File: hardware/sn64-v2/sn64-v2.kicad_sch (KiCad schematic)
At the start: 0 parts

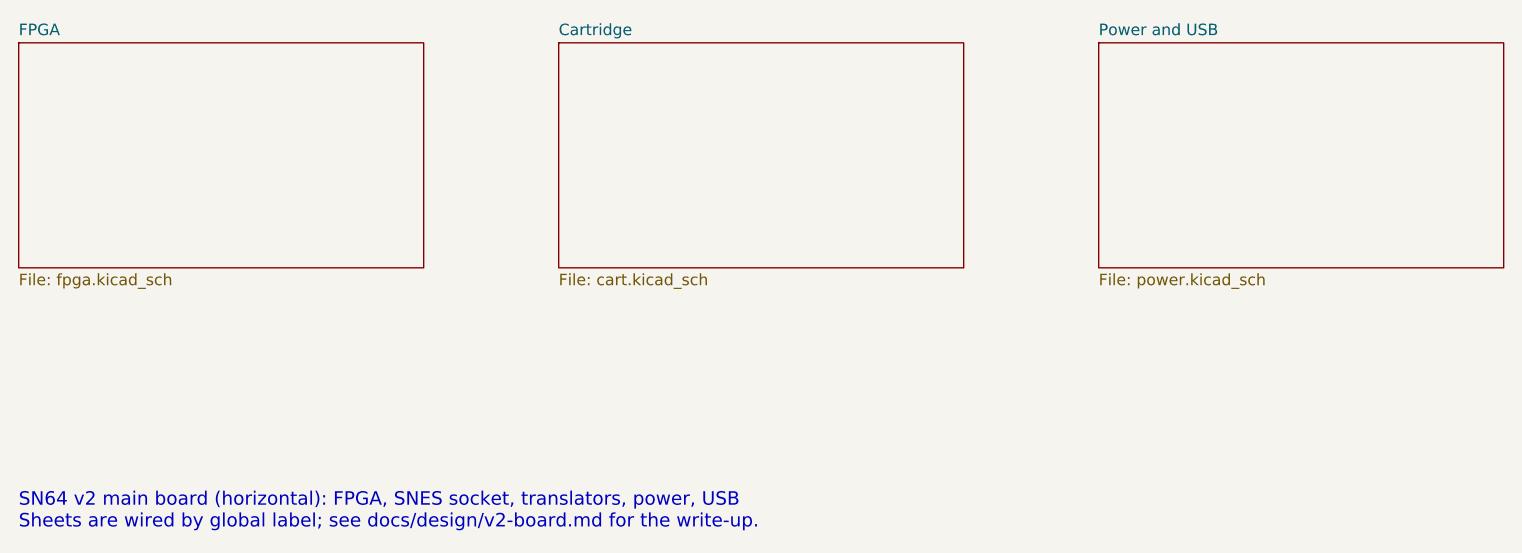
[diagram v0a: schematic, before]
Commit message: v2 single board: routed board, schematic with the N64 edge, validation reports, renders and notes
Co-Authored-By: Claude Fable 5.1 <noreply@anthropic.com>
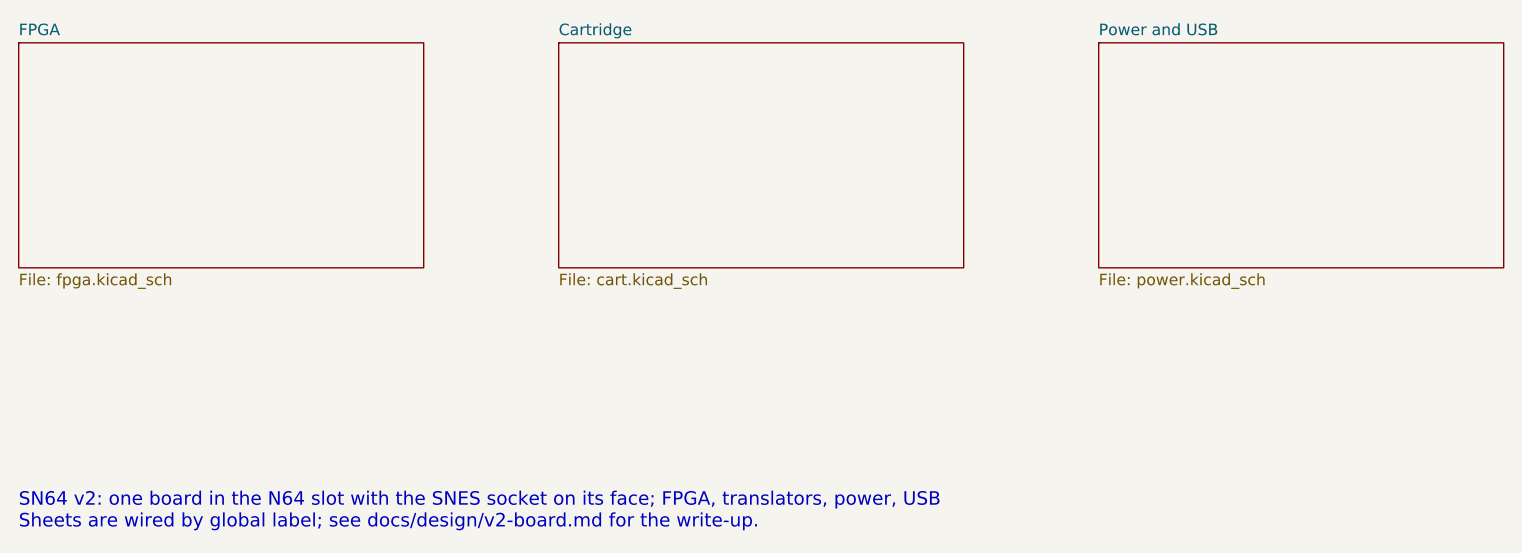
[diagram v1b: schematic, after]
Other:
- note added: "SN64 v2: one board in the N64 slot with the SNES socket on its face; FPGA, translators, power, USB Sheets are wired by global label; see docs/design/v2-board.md for the write-up."
- note removed: "SN64 v2 main board (horizontal): FPGA, SNES socket, translators, power, USB Sheets are wired by global label; see docs/design/v2-board.md for the write-up."
- title: SN64 v2 main board (horizontal): FPGA, SNES socket, translators, power, USB -> SN64 v2: one board in the N64 slot with the SNES socket on its face; FPGA, translators, power, USB
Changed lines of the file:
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@@
-(kicad_sch (version 20250114) (generator "sn64_v2_authoring") (generator_version "10.0") (paper "A4") (title_block (title "SN64 v2 main board (horizontal): FPGA, SNES socket, translators, power, USB") (date "2026-09-30") (rev "v2 draft 0.1") (comment 1 "DESIGN DRAFT - NOT FOR MANUFACTURE"))
+(kicad_sch (version 20250114) (generator "sn64_v2_authoring") (generator_version "10.0") (paper "A4") (title_block (title "SN64 v2: one board in the N64 slot with the SNES socket on its face; FPGA, translators, power, USB") (date "2026-09-30") (rev "v2 draft 0.1") (comment 1 "DESIGN DRAFT - NOT FOR MANUFACTURE"))
 (sheet (at 30 40) (size 45 25) (exclude_from_sim no) (in_bom yes) (on_board yes) (dnp no) (fields_autoplaced yes) (stroke (width 0.1524) (type solid)) (fill (color 0 0 0 0.0000)) (property "Sheetname" "FPGA" (at 30 39.3 0) (effects (font (size 1.27 1.27)) (justify left bottom))) (property "Sheetfile" "fpga.kicad_sch" (at 30 65.6 0) (effects (font (size 1.27 1.27)) (justify left top))) (instances (project "sn64-v2" (path "/d28f46aa-91c7-5060-a563-bf74d208e51e" (page "2")))))
 (sheet (at 90 40) (size 45 25) (exclude_from_sim no) (in_bom yes) (on_board yes) (dnp no) (fields_autoplaced yes) (stroke (width 0.1524) (type solid)) (fill (color 0 0 0 0.0000)) (property "Sheetname" "Cartridge" (at 90 39.3 0) (effects (font (size 1.27 1.27)) (justify left bottom))) (property "Sheetfile" "cart.kicad_sch" (at 90 65.6 0) (effects (font (size 1.27 1.27)) (justify left top))) (instances (project "sn64-v2" (path "/d28f46aa-91c7-5060-a563-bf74d208e51e" (page "3")))))
 (sheet (at 150 40) (size 45 25) (exclude_from_sim no) (in_bom yes) (on_board yes) (dnp no) (fields_autoplaced yes) (stroke (width 0.1524) (type solid)) (fill (color 0 0 0 0.0000)) (property "Sheetname" "Power and USB" (at 150 39.3 0) (effects (font (size 1.27 1.27)) (justify left bottom))) (property "Sheetfile" "power.kicad_sch" (at 150 65.6 0) (effects (font (size 1.27 1.27)) (justify left top))) (instances (project "sn64-v2" (path "/d28f46aa-91c7-5060-a563-bf74d208e51e" (page "4")))))
-(text "SN64 v2 main board (horizontal): FPGA, SNES socket, translators, power, USB\nSheets are wired by global label; see docs/design/v2-board.md for the write-up." (exclude_from_sim no) (at 30 90 0) (effects (font (size 1.5 1.5)) (justify left top)))
+(text "SN64 v2: one board in the N64 slot with the SNES socket on its face; FPGA, translators, power, USB\nSheets are wired by global label; see docs/design/v2-board.md for the write-up." (exclude_from_sim no) (at 30 90 0) (effects (font (size 1.5 1.5)) (justify left top)))
 (sheet_instances (path "/" (page "1"))) (embedded_fonts no))
